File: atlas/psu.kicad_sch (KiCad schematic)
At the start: 25 parts

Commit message: sensor supply
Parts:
- added C? (x3): 1u, symbol Device:C
- added C? (x3): C, symbol Device:C
- added D?: D_Schottky, symbol Device:D_Schottky
- added U? (x3): TLS115D0EJ, symbol tls115:TLS115D0EJ
- L?: value L -> 10u
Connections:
- net +5V: now also U?.5 (ADJ), U?.5 (ADJ), U?.5 (ADJ)
- net 12V_PROT: now also C?.1, C?.1, C?.1, U?.8 (IN), U?.8 (IN), U?.8 (IN)
- net GND: now also C?.2, C?.2, C?.2, C?.2, C?.2, C?.2, D?.2 (A), U?.3 (GND), U?.3 (GND), U?.3 (GND), U?.9 (GND), U?.9 (GND), U?.9 (GND)
- net at C?.2, L?.1, U?.8 (SW): now also D?.1 (K)
- net REG_EN: now reaches C?.1, D?.1 (K), R?.1, R?.2, U?.3 (EN)
- net REG_EN: now also U?.7 (EN), U?.7 (EN), U?.7 (EN)
- new net 5V_SENSOR_1: C?.1, U?.1 (OUT)
- new net 5V_SENSOR_2: C?.1, U?.1 (OUT)
- new net 5V_SENSOR_3: C?.1, U?.1 (OUT)
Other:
- note added: "12V_IGN is expected to have voltage applied only when the user actually wants the engine to be able to run."
- note added: "12V_PERMANENT is expected to always have voltage applied, even when the key is off."
- note added: "5v Sensor Supplies (x3)"
- note added: "Input Filter & 5v Regulator"
- note added: "Load Dump + Reverse Protection"
- moved on the sheet: C?, D?, L?, R?, U?

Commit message: progress
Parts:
- added C?: 10u, symbol Device:C
- added U?: TPS70933DBV, Package_TO_SOT_SMD:SOT-23-5, symbol Regulator_Linear:TPS78233DDC
- C? (x5): footprint (none) -> Capacitor_SMD:C_0603_1608Metric; LCSC (none) -> C15849
- C? (x3): value C -> 1u; footprint (none) -> Capacitor_SMD:C_0603_1608Metric; LCSC (none) -> C15849
- C?: footprint (none) -> Capacitor_SMD:C_0402_1005Metric; LCSC (none) -> C1525
- D?: footprint (none) -> Diode_SMD:D_MiniMELF; LCSC (none) -> C8062
- R?: footprint (none) -> Capacitor_SMD:C_0402_1005Metric; LCSC (none) -> C36871
- R?: footprint (none) -> Capacitor_SMD:C_0402_1005Metric; LCSC (none) -> C25125
- R?: footprint (none) -> Capacitor_SMD:C_0402_1005Metric; LCSC (none) -> C25752
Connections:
- net 12V_PROT: now also U?.1 (IN), U?.3 (EN)
- net GND: now also C?.2, U?.2 (GND), U?.4 (GND)
- new net V_STANDBY: C?.1, U?.5 (OUT)

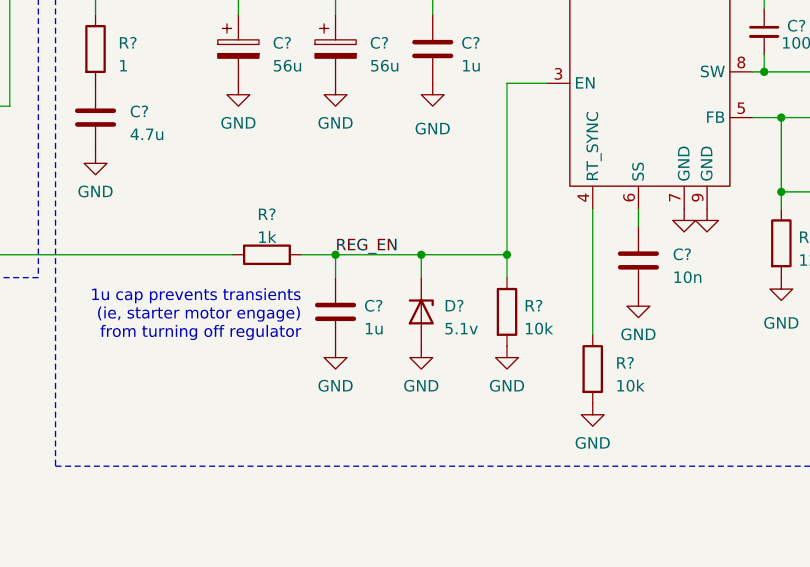
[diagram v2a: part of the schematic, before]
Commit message: assign some components
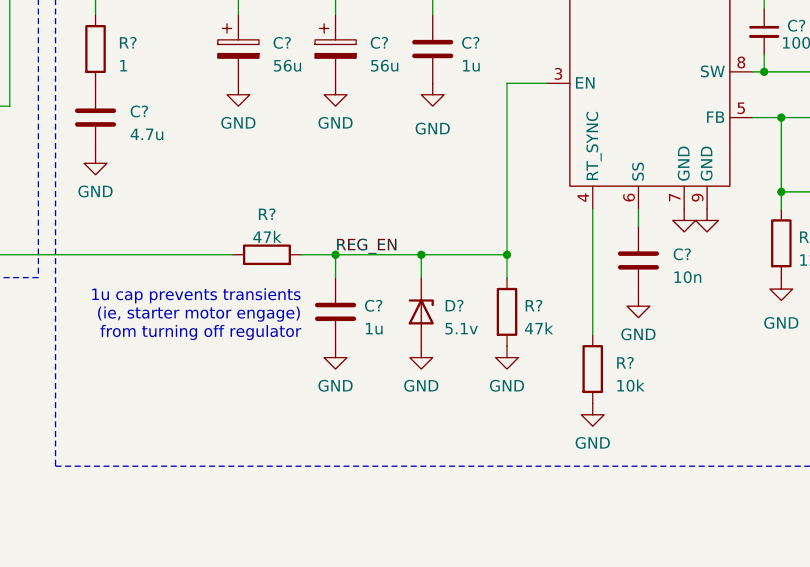
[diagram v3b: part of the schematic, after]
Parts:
- C? (x2): footprint (none) -> Capacitor_Tantalum_SMD:CP_EIA-3528-15_AVX-H; LCSC (none) -> C139576
- C?: footprint (none) -> Capacitor_SMD:C_1206_3216Metric; LCSC (none) -> C29823
- D? (x2): footprint (none) -> Diode_SMD:D_SMA; LCSC (none) -> C22452
- D? (x2): footprint (none) -> Diode_SMD:D_SMC; LCSC (none) -> C133648
- D?: value D_Schottky -> 47k; footprint (none) -> Diode_SMD:D_SMA; LCSC (none) -> C22452
- R?: value 1k -> 47k; footprint (none) -> Resistor_SMD:R_0603_1608Metric; LCSC (none) -> C25819
- R?: value 10k -> 47k; footprint (none) -> Resistor_SMD:R_0603_1608Metric; LCSC (none) -> C25819
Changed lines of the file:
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@@
     (in_bom yes) (on_board yes) (fields_autoplaced)
     (property "Reference" "R?" (id 0) (at 109.855 60.96 90))
-    (property "Value" "1k" (id 1) (at 109.855 63.5 90))
-    (property "Footprint" "" (id 2) (at 109.855 67.183 90)
+    (property "Value" "47k" (id 1) (at 109.855 63.5 90))
+    (property "Footprint" "Resistor_SMD:R_0603_1608Metric" (id 2) (at 109.855 67.183 90)
       (effects (font (size 1.27 1.27)) hide)
     )
@@
       (effects (font (size 1.27 1.27)) hide)
     )
+    (property "LCSC" "C25819" (id 4) (at 109.855 65.405 0)
+      (effects (font (size 1.27 1.27)) hide)
+    )
     (pin "1")
     (pin "2")
@@
       (effects (font (size 1.27 1.27)) (justify left))
     )
-    (property "Value" "10k" (id 1) (at 138.43 73.6599 0)
-      (effects (font (size 1.27 1.27)) (justify left))
-    )
-    (property "Footprint" "" (id 2) (at 134.747 71.755 90)
+    (property "Value" "47k" (id 1) (at 138.43 73.6599 0)
+      (effects (font (size 1.27 1.27)) (justify left))
+    )
+    (property "Footprint" "Resistor_SMD:R_0603_1608Metric" (id 2) (at 134.747 71.755 90)
       (effects (font (size 1.27 1.27)) hide)
     )
     (property "Datasheet" "~" (id 3) (at 136.525 71.755 0)
+      (effects (font (size 1.27 1.27)) hide)
+    )
+    (property "LCSC" "C25819" (id 4) (at 136.525 71.755 0)
       (effects (font (size 1.27 1.27)) hide)
     )
@@
       (effects (font (size 1.27 1.27)) (justify right))
     )
-    (property "Footprint" "" (id 2) (at 54.61 41.275 0)
+    (property "Footprint" "Diode_SMD:D_SMC" (id 2) (at 54.61 41.275 0)
       (effects (font (size 1.27 1.27)) hide)
     )
     (property "Datasheet" "~" (id 3) (at 54.61 41.275 0)
+      (effects (font (size 1.27 1.27)) hide)
+    )
+    (property "LCSC" "C133648" (id 4) (at 54.61 41.275 0)
       (effects (font (size 1.27 1.27)) hide)
     )
@@
       (effects (font (size 1.27 1.27)) (justify right))
     )
-    (property "Footprint" "" (id 2) (at 54.61 53.975 0)
+    (property "Footprint" "Diode_SMD:D_SMC" (id 2) (at 54.61 53.975 0)
       (effects (font (size 1.27 1.27)) hide)
     )
     (property "Datasheet" "~" (id 3) (at 54.61 53.975 0)
+      (effects (font (size 1.27 1.27)) hide)
+    )
+    (property "LCSC" "C133648" (id 4) (at 54.61 53.975 0)
       (effects (font (size 1.27 1.27)) hide)
     )
@@
     (property "Reference" "D?" (id 0) (at 71.755 30.48 0))
     (property "Value" "D_Schottky" (id 1) (at 71.755 33.02 0))
-    (property "Footprint" "" (id 2) (at 71.755 36.195 0)
+    (property "Footprint" "Diode_SMD:D_SMA" (id 2) (at 71.755 36.195 0)
       (effects (font (size 1.27 1.27)) hide)
     )
     (property "Datasheet" "~" (id 3) (at 71.755 36.195 0)
+      (effects (font (size 1.27 1.27)) hide)
+    )
+    (property "LCSC" "C22452" (id 4) (at 71.755 36.195 0)
       (effects (font (size 1.27 1.27)) hide)
     )
@@
     (property "Reference" "D?" (id 0) (at 71.755 43.18 0))
     (property "Value" "D_Schottky" (id 1) (at 71.755 45.72 0))
-    (property "Footprint" "" (id 2) (at 71.755 48.895 0)
+    (property "Footprint" "Diode_SMD:D_SMA" (id 2) (at 71.755 48.895 0)
       (effects (font (size 1.27 1.27)) hide)
     )
     (property "Datasheet" "~" (id 3) (at 71.755 48.895 0)
+      (effects (font (size 1.27 1.27)) hide)
+    )
+    (property "LCSC" "C22452" (id 4) (at 71.755 48.895 0)
       (effects (font (size 1.27 1.27)) hide)
     )
@@
       (effects (font (size 1.27 1.27)) (justify right))
     )
-    (property "Value" "D_Schottky" (id 1) (at 177.8 40.6399 90)
+    (property "Value" "47k" (id 1) (at 177.8 40.6399 90)
       (effects (font (size 1.27 1.27)) (justify right) hide)
     )
-    (property "Footprint" "" (id 2) (at 174.625 38.735 0)
+    (property "Footprint" "Diode_SMD:D_SMA" (id 2) (at 174.625 38.735 0)
       (effects (font (size 1.27 1.27)) hide)
     )
@@
       (effects (font (size 1.27 1.27)) hide)
     )
+    (property "LCSC" "C22452" (id 4) (at 174.625 38.735 0)
+      (effects (font (size 1.27 1.27)) hide)
+    )
     (pin "1")
     (pin "2")
@@
       (effects (font (size 1.27 1.27)) (justify left))
     )
-    (property "Footprint" "" (id 2) (at 91.7702 53.975 0)
+    (property "Footprint" "Capacitor_SMD:C_1206_3216Metric" (id 2) (at 91.7702 53.975 0)
       (effects (font (size 1.27 1.27)) hide)
     )
     (property "Datasheet" "~" (id 3) (at 90.805 50.165 0)
+      (effects (font (size 1.27 1.27)) hide)
+    )
+    (property "LCSC" "C29823" (id 4) (at 90.805 50.165 0)
       (effects (font (size 1.27 1.27)) hide)
     )
@@
       (effects (font (size 1.27 1.27)) (justify left))
     )
-    (property "Footprint" "" (id 2) (at 207.3402 55.245 0)
+    (property "Footprint" "Capacitor_Tantalum_SMD:CP_EIA-3528-15_AVX-H" (id 2) (at 207.3402 55.245 0)
       (effects (font (size 1.27 1.27)) hide)
     )
@@
       (effects (font (size 1.27 1.27)) hide)
     )
+    (property "LCSC" "C139576" (id 4) (at 206.375 51.435 0)
+      (effects (font (size 1.27 1.27)) hide)
+    )
     (pin "1")
     (pin "2")
@@
       (effects (font (size 1.27 1.27)) (justify left))
     )
-    (property "Footprint" "" (id 2) (at 218.1352 55.245 0)
+    (property "Footprint" "Capacitor_Tantalum_SMD:CP_EIA-3528-15_AVX-H" (id 2) (at 218.1352 55.245 0)
       (effects (font (size 1.27 1.27)) hide)
     )
@@
       (effects (font (size 1.27 1.27)) hide)
     )
+    (property "LCSC" "C139576" (id 4) (at 217.17 51.435 0)
+      (effects (font (size 1.27 1.27)) hide)
+    )

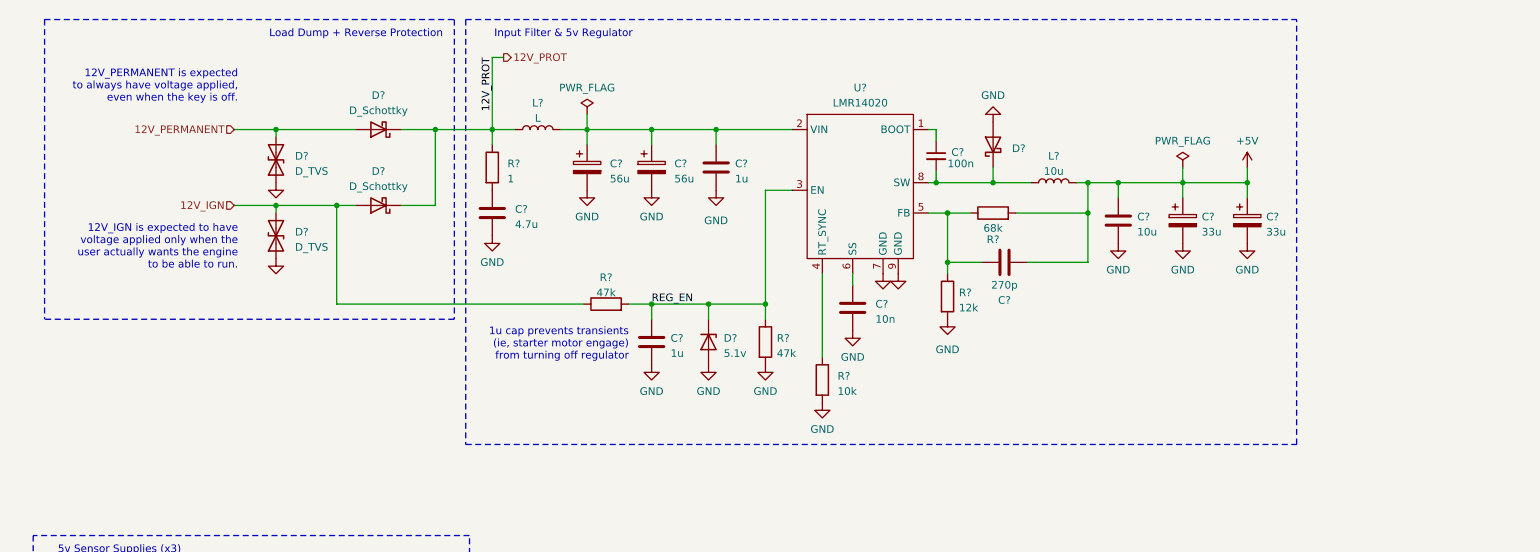
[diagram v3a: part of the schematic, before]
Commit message: bigger load dump diodes
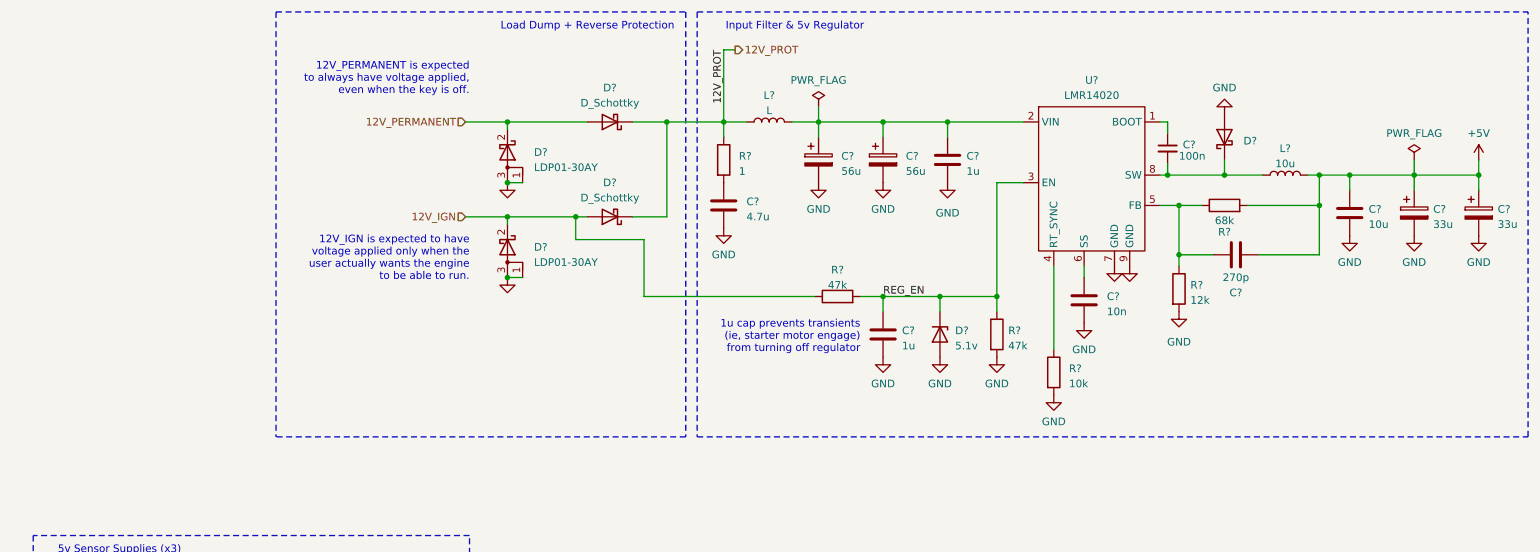
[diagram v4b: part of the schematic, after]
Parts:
- removed D? (x2): D_TVS, Diode_SMD:D_SMC, symbol Device:D_TVS
- added D? (x2): LDP01-30AY, Package_TO_SOT_SMD:TO-252-2, symbol Device:D_Schottky_AKA
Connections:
- net 12V_IGN: now also D?.2 (K)
- net 12V_PERMANENT: now also D?.2 (K)
- net GND: now also D?.1 (A), D?.1 (A), D?.3 (A), D?.3 (A)
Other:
- moved on the sheet: C?, D?, L?, R?, U?

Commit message: progress
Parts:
- R204: renamed from R?; footprint (none) -> Resistor_SMD:R_0402_1005Metric; LCSC (none) -> C25744
- U205: renamed from U?; LCSC (none) -> C187824
- gave numbers to parts that had none: 35
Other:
- title: (none) -> rusEFI ATLAS

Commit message: progressssss
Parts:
- removed C217, C218: 33u, Capacitor_Tantalum_SMD:CP_EIA-3528-15_AVX-H, symbol Device:C_Polarized
- added C217, C218: 10u, Capacitor_SMD:C_1206_3216Metric, symbol Device:C
- added C? (x2): 56u, symbol Device:C_Polarized
- added D?: 5.1v, Diode_SMD:D_MiniMELF, symbol Device:D_Zener
- added Q?: 2N7002, Package_TO_SOT_SMD:SOT-23, symbol Device:Q_NMOS_GSD
- added Q?: IRLR3636, symbol Device:Q_PMOS_GDS
- added R?: 1k, symbol Device:R
- C207, C216: footprint (none) -> Capacitor_SMD:C_1206_3216Metric; LCSC (none) -> C13585
- C213: footprint (none) -> Capacitor_SMD:C_0603_1608Metric; LCSC (none) -> C57112
- U205: footprint (none) -> Package_SO:SOIC-8-1EP_3.9x4.9mm_P1.27mm_EP2.41x3.3mm
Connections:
- net +5V: now also C217.1, C218.1
- net 12V_PERMANENT: now also Q?.2 (D)
- net GND: now also C217.2, C218.2, C?.2, C?.2, Q?.2 (S)
- net REG_EN: now also Q?.1 (G)
- new net: C?.1, C?.1, D?.1 (K), Q?.3 (S)
- new net: D?.2 (A), Q?.1 (G), R?.1
- new net: Q?.3 (D), R?.2
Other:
- moved on the sheet: C201, C202, C203, C204, C205, C206, C207, C208, C209, C210, C211, C212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

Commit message: hellen modules
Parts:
- added Q203: IRLR3636, Package_TO_SOT_SMD:TO-252-2, symbol Device:Q_PMOS_GDS
- added R208: 10k, symbol Device:R
- Q202: renamed from Q?; footprint (none) -> Package_TO_SOT_SMD:TO-252-2
- gave numbers to parts that had none: 5
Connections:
- net at D207.1 (K), Q202.3 (S): now also Q203.3 (S), R208.1; no longer C219.1, C220.1
- net at D207.2 (A), Q202.1 (G), R207.1: now also Q203.1 (G), R208.2
- new net 12V_POWER: C219.1, C220.1, Q203.2 (D)
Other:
- note added: "for ETB, high sides, freewheel diodes, etc"
- moved on the sheet: C219, C220, D207, Q201, Q202, R207
